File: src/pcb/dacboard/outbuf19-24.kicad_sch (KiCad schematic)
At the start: 18 parts, among them U77 AD8675ARZ, U78 AD8675ARZ, U79 AD8675ARZ, U80 AD8675ARZ, U81 AD8675ARZ, U82 AD8675ARZ

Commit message: dacboard routing
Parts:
- C65, C66, C67, C68, C69, C70: footprint (none) -> Capacitor_SMD:C_0603_1608Metric_Pad1.08x0.95mm_HandSolder
- R34, R35, R36, R37, R38, R39: footprint (none) -> Resistor_SMD:R_0805_2012Metric
- U77, U78, U79, U80, U81, U82: footprint R_8_ADI -> Package_SO:SOIC-8_3.9x4.9mm_P1.27mm
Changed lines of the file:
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@@
 			)
 		)
-		(property "Footprint" ""
+		(property "Footprint" "Resistor_SMD:R_0805_2012Metric"
 			(at 129.794 47.244 90)
 			(effects
@@
 			)
 		)
-		(property "Footprint" ""
+		(property "Footprint" "Resistor_SMD:R_0805_2012Metric"
 			(at 260.604 123.444 90)
 			(effects
@@
 			)
 		)
-		(property "Footprint" ""
+		(property "Footprint" "Capacitor_SMD:C_0603_1608Metric_Pad1.08x0.95mm_HandSolder"
 			(at 37.7952 90.17 0)
 			(effects
@@
 			)
 		)
-		(property "Footprint" ""
+		(property "Footprint" "Resistor_SMD:R_0805_2012Metric"
 			(at 129.794 125.984 90)
 			(effects
@@
 			)
 		)
-		(property "Footprint" ""
+		(property "Footprint" "Capacitor_SMD:C_0603_1608Metric_Pad1.08x0.95mm_HandSolder"
 			(at 168.6052 129.54 0)
 			(effects
@@
 			)
 		)
-		(property "Footprint" "R_8_ADI"
+		(property "Footprint" "Package_SO:SOIC-8_3.9x4.9mm_P1.27mm"
 			(at 54.61 80.01 0)
 			(effects
@@
 			)
 		)
-		(property "Footprint" ""
+		(property "Footprint" "Resistor_SMD:R_0805_2012Metric"
 			(at 260.604 47.244 90)
 			(effects
@@
 			)
 		)
-		(property "Footprint" "R_8_ADI"
+		(property "Footprint" "Package_SO:SOIC-8_3.9x4.9mm_P1.27mm"
 			(at 54.61 121.92 0)
 			(effects
@@
 			)
 		)
-		(property "Footprint" ""
+		(property "Footprint" "Resistor_SMD:R_0805_2012Metric"
 			(at 260.604 84.074 90)
 			(effects
@@
 			)
 		)
-		(property "Footprint" "R_8_ADI"
+		(property "Footprint" "Package_SO:SOIC-8_3.9x4.9mm_P1.27mm"
 			(at 185.42 119.38 0)
 			(effects
@@
 			)
 		)
-		(property "Footprint" ""
+		(property "Footprint" "Capacitor_SMD:C_0603_1608Metric_Pad1.08x0.95mm_HandSolder"
 			(at 168.6052 90.17 0)
 			(effects
@@
 			)
 		)
-		(property "Footprint" ""
+		(property "Footprint" "Capacitor_SMD:C_0603_1608Metric_Pad1.08x0.95mm_HandSolder"
 			(at 168.6052 53.34 0)
 			(effects
@@
 			)
 		)
-		(property "Footprint" ""
+		(property "Footprint" "Capacitor_SMD:C_0603_1608Metric_Pad1.08x0.95mm_HandSolder"
 			(at 37.7952 132.08 0)
 			(effects
@@
 			)
 		)
-		(property "Footprint" "R_8_ADI"
+		(property "Footprint" "Package_SO:SOIC-8_3.9x4.9mm_P1.27mm"
 			(at 185.42 80.01 0)
 			(effects
@@
 			)
 		)
-		(property "Footprint" ""
+		(property "Footprint" "Resistor_SMD:R_0805_2012Metric"
 			(at 129.794 84.074 90)
 			(effects
@@
 			)
 		)
-		(property "Footprint" ""
+		(property "Footprint" "Capacitor_SMD:C_0603_1608Metric_Pad1.08x0.95mm_HandSolder"
 			(at 37.7952 53.34 0)
 			(effects
@@
 			)
 		)
-		(property "Footprint" "R_8_ADI"
+		(property "Footprint" "Package_SO:SOIC-8_3.9x4.9mm_P1.27mm"
 			(at 54.61 43.18 0)
 			(effects
@@
 			)
 		)
-		(property "Footprint" "R_8_ADI"
+		(property "Footprint" "Package_SO:SOIC-8_3.9x4.9mm_P1.27mm"
 			(at 185.42 43.18 0)
 			(effects

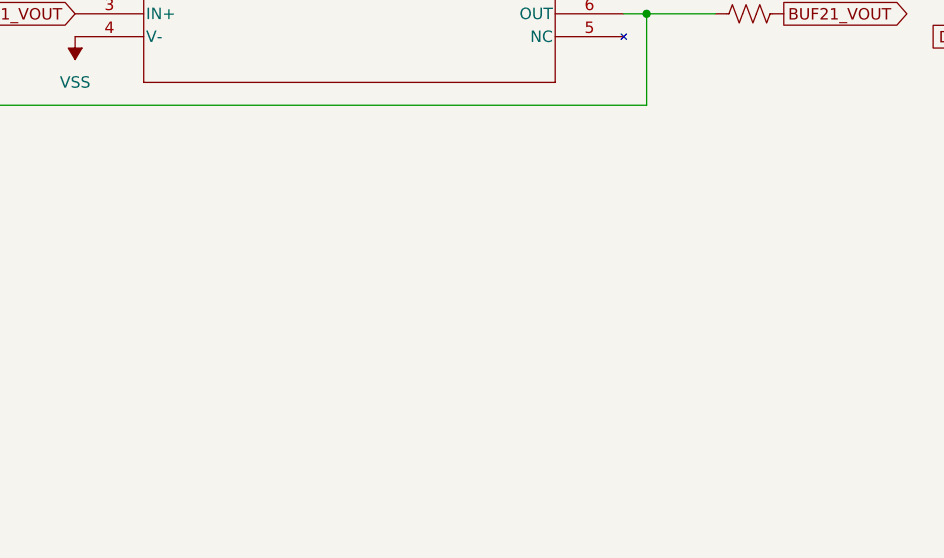
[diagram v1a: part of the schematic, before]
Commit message: got rid of all drc errors
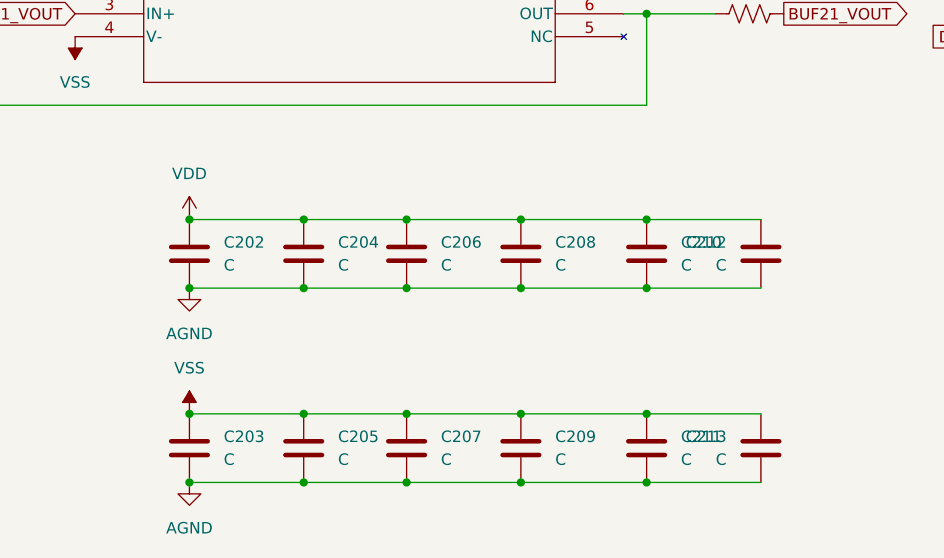
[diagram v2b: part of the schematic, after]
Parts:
- added C202, C203, C204, C205, C206, C207, C208, C209, C210, C211, C212, C213: C, Capacitor_SMD:C_0402_1005Metric_Pad0.74x0.62mm_HandSolder, symbol Device:C
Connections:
- net VDD: now also C202.1, C204.1, C206.1, C208.1, C210.1, C212.1
- net VSS: now also C203.1, C205.1, C207.1, C209.1, C211.1, C213.1
- new net AGND: C202.2, C203.2, C204.2, C205.2, C206.2, C207.2, C208.2, C209.2, C210.2, C211.2, C212.2, C213.2
